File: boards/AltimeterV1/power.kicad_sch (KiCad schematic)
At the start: 36 parts

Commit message: updated hierarchical sheets and moved power schematics
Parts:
- removed BT?: Flight Computer Battery, Connector_JST:JST_PH_B2B-PH-K_1x02_P2.00mm_Vertical, symbol Device:Battery_Cell
- removed C?: 10uF, Capacitor_SMD:C_0805_2012Metric, symbol Device:C_Polarized_US
- removed C?: 2.2nF, Capacitor_SMD:C_0603_1608Metric, symbol Device:C
- removed C?: 2.27nF, Capacitor_SMD:C_0603_1608Metric, symbol Device:C
- removed C?: ~, Capacitor_SMD:C_0603_1608Metric, symbol Device:C
- removed C? (x2): 4.7u, Capacitor_SMD:C_0603_1608Metric, symbol Device:C
- removed C?: 47uF, Capacitor_SMD:C_0603_1608Metric, symbol Device:C
- removed C?, CByp?, CReg?, Cref?: 1uF, Capacitor_SMD:C_0603_1608Metric, symbol Device:C
- removed D? (x2): LED, LED_SMD:LED_0603_1608Metric, symbol Device:LED
- removed D?: D, Diode_SMD:D_0603_1608Metric, symbol Device:D
- removed D?: GREEN, LED_SMD:LED_0603_1608Metric, symbol Device:LED
- removed J?: TE_1776113-3, TerminalBlock_TE:TE_1776113-3, symbol Connector:Screw_Terminal_01x03
- removed R? (x4): 10k, Resistor_SMD:R_0603_1608Metric, symbol Device:R_US
- removed R?: 1k33, Resistor_SMD:R_0603_1608Metric, symbol Device:R_US
- removed R?: 432k, Resistor_SMD:R_0603_1608Metric, symbol Device:R_US
- removed R?: 5k6, Resistor_SMD:R_0603_1608Metric, symbol Device:R_US
- removed R?: 470k, Resistor_SMD:R_0603_1608Metric, symbol Device:R_US
- removed R?: 80k6, Resistor_SMD:R_0603_1608Metric, symbol Device:R_US
- removed R? (x3): 1k, Resistor_SMD:R_0603_1608Metric, symbol Device:R_US
- removed R?: 100k, Resistor_SMD:R_0603_1608Metric, symbol Device:R_US
- removed R?: 8.06k, Resistor_SMD:R_0603_1608Metric, symbol Device:R_US
- removed R?: 9.09k, Resistor_SMD:R_0603_1608Metric, symbol Device:R_US
- removed R?: 47k, Resistor_SMD:R_0603_1608Metric, symbol Device:R_US
- removed U?: ADP7158ACPZ-3.3-R7, Regulator_Linear:ADP7158ACPZ-3.3-R7, symbol regulator_analog:ADP7158ACPZ-3.3-R7
- removed U?: MCP73831-2-OT, Package_TO_SOT_SMD:SOT-23-5, symbol Battery_Management:MCP73831-2-OT
- removed U?: TPS2521, EFuse_Texas:TPS25210LRPWR, symbol Efuse_Texas_TPS2521:TPS2521
- added C? (x2): 1uF, Capacitor_SMD:C_0805_2012Metric, symbol D24V50F5:C
- added C?: 10nF, Capacitor_SMD:C_0805_2012Metric, symbol D24V50F5:C
- added J?: Conn_01x02_Female, symbol Connector:Conn_01x02_Female
- added U?: LD3985M33R_SOT23, Package_TO_SOT_SMD:SOT-23-5, symbol Regulator_Linear:LD3985M33R_SOT23
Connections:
- net +3V3: now also C?.1, U?.5 (VOUT)
- net GND: now also C?.1, C?.2, C?.2, J?.2 (Pin_2), U?.2 (GND)
- new net: C?.2, U?.4 (BYP)
- new net VBAT: C?.1, U?.1 (VIN)
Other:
- note added: "LD39 Linear Voltage Regulator"
- note added: "VBAT"
- note removed: "2.3V to 5.5V Input 3.3V Output"
- note removed: "2A Max Load"
- note removed: "Battery Switch Terminal"
- note removed: "Charger"
- note removed: "E-Fuse"
- note removed: "EN/UVLO must have large pullup resistor to prevent current leakage during reverse polarity. (350k or higher)"
- note removed: "Flight Battery Voltage Sensing"
- note removed: "Max Rating: Vin to GND = -0.3V to +7V"
- note removed: "OLD ALTIMETER POWER CIRCUIS"
- note removed: "OVCSEL Clamp Threshold Properties GND = 3.8V Open = 5.7V"
- note removed: "Protects: -15V to 28V Operates: 2.53V to 5.7V, 2.3A PowerGood Signal: V_IN > 2.7V"
- note removed: "Regulator"
- note removed: "Use calculator in datasheet for component values."
- note removed: "review resistance value choice with team (on 10k resistor)"

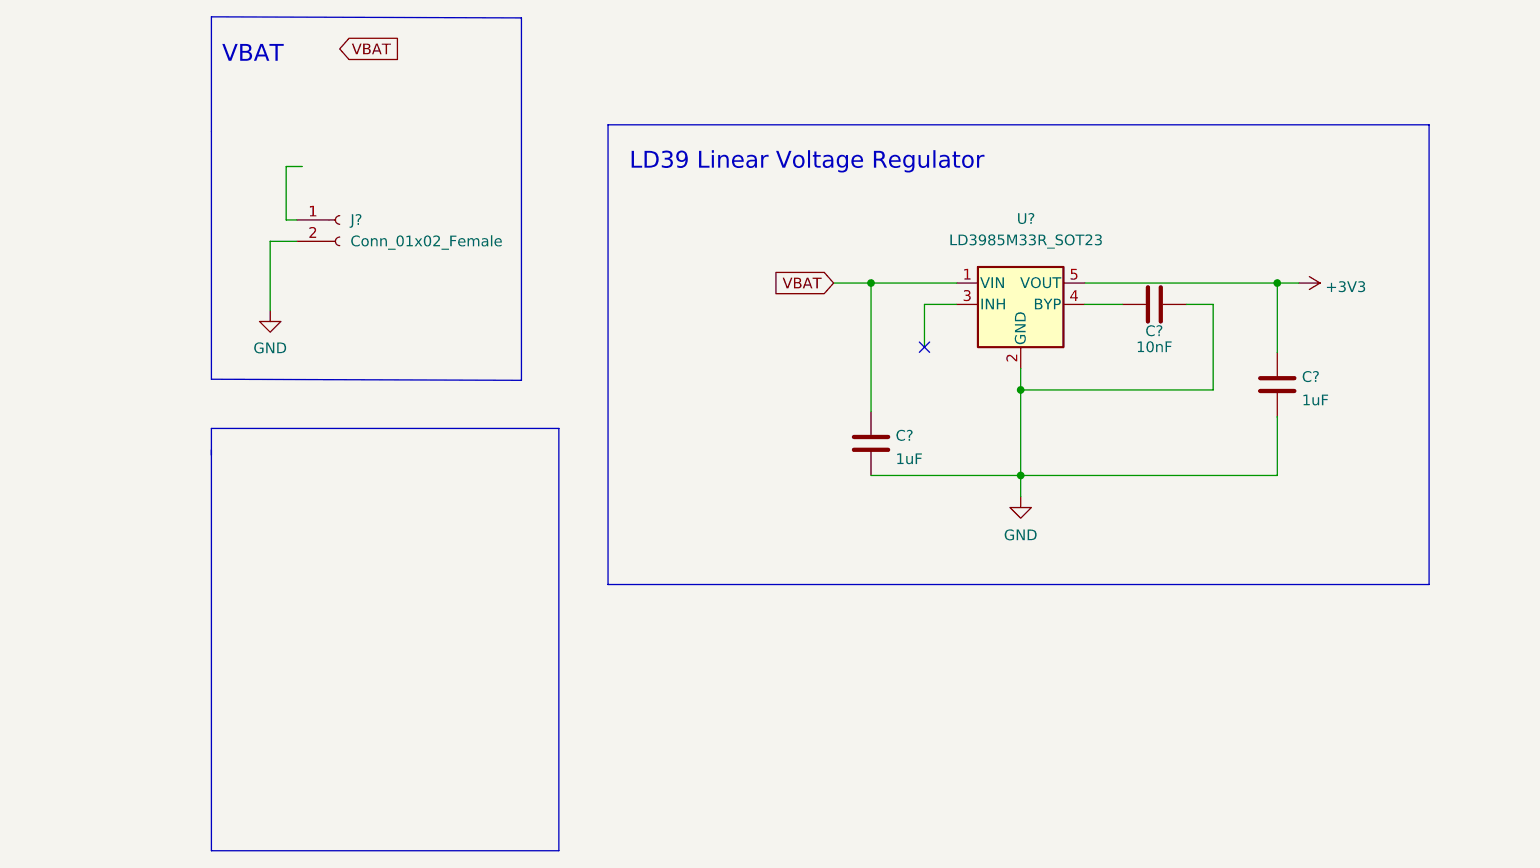
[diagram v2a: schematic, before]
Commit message: updated all schematics, and removed hierarchical sheets
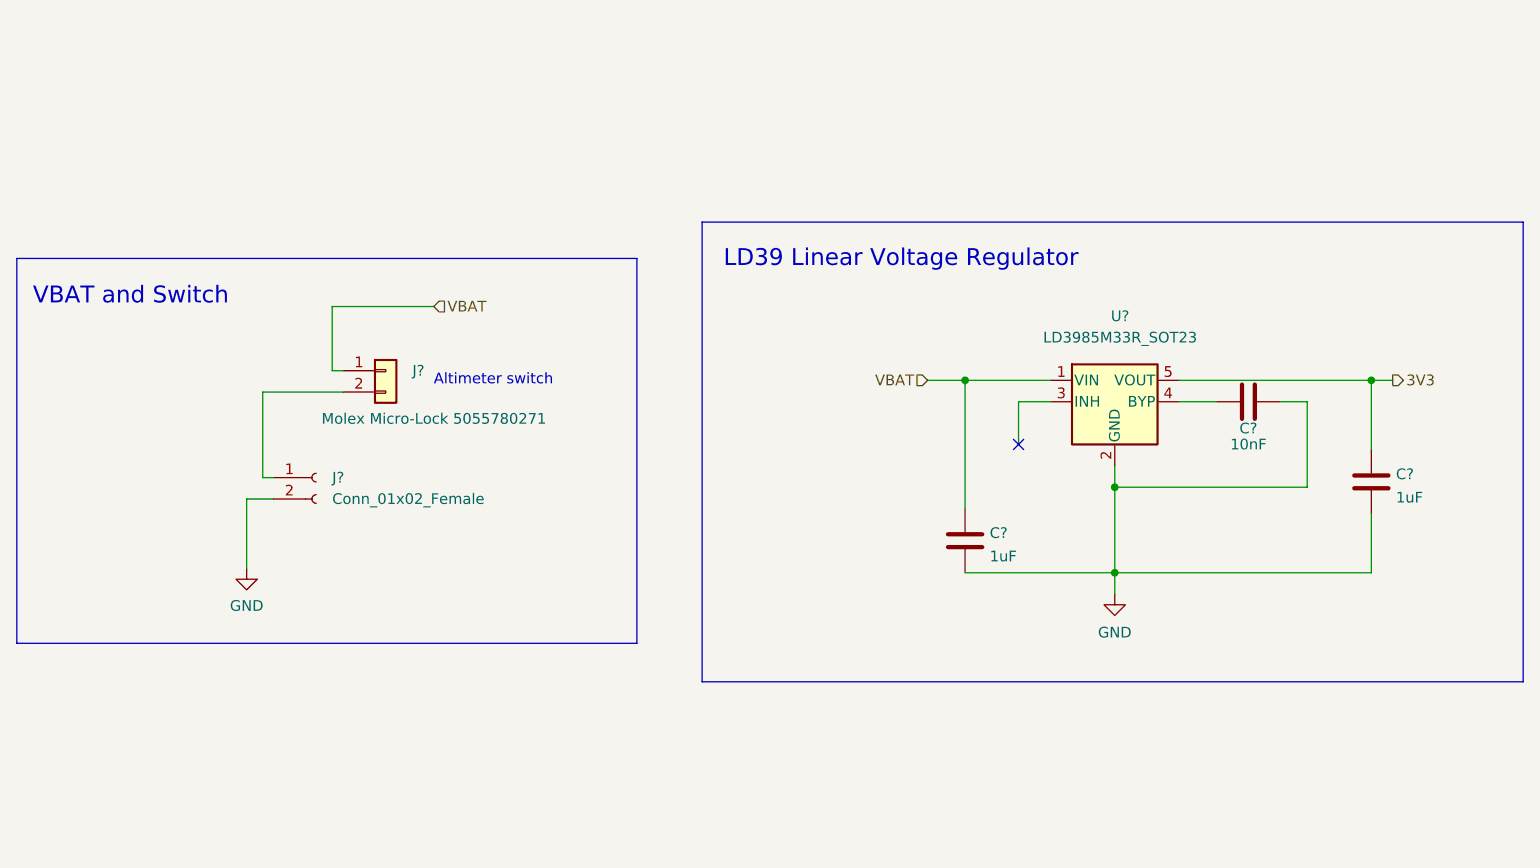
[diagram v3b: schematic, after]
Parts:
- added J?: Molex Micro-Lock 5055780271, Connector_Molex:Molex_CLIK-Mate_502494-0270_1x02-1MP_P2.00mm_Horizontal, symbol Connector_Generic:Conn_01x02
- J?: footprint (none) -> Connector_JST:JST_PH_B2B-PH-K_1x02_P2.00mm_Vertical
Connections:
- net VBAT: now also J?.1 (Pin_1)
- net at J?.1 (Pin_1): now also J?.2 (Pin_2)
- net +3V3 renamed 3V3
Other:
- note added: "Altimeter switch"
- note added: "VBAT and Switch"
- note removed: "VBAT"
- moved on the sheet: C?, J?, U?

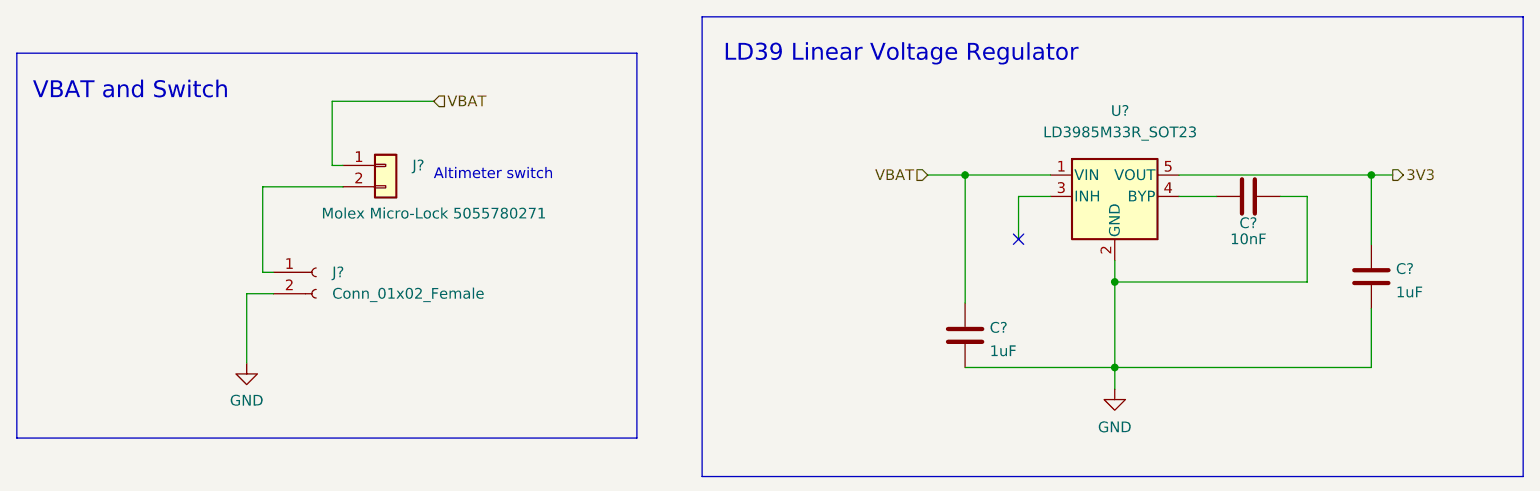
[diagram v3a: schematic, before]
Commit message: added flash memory, added buzzer, corrected all schematic labels, assigned footprints, added switch, updated pcb from schematic
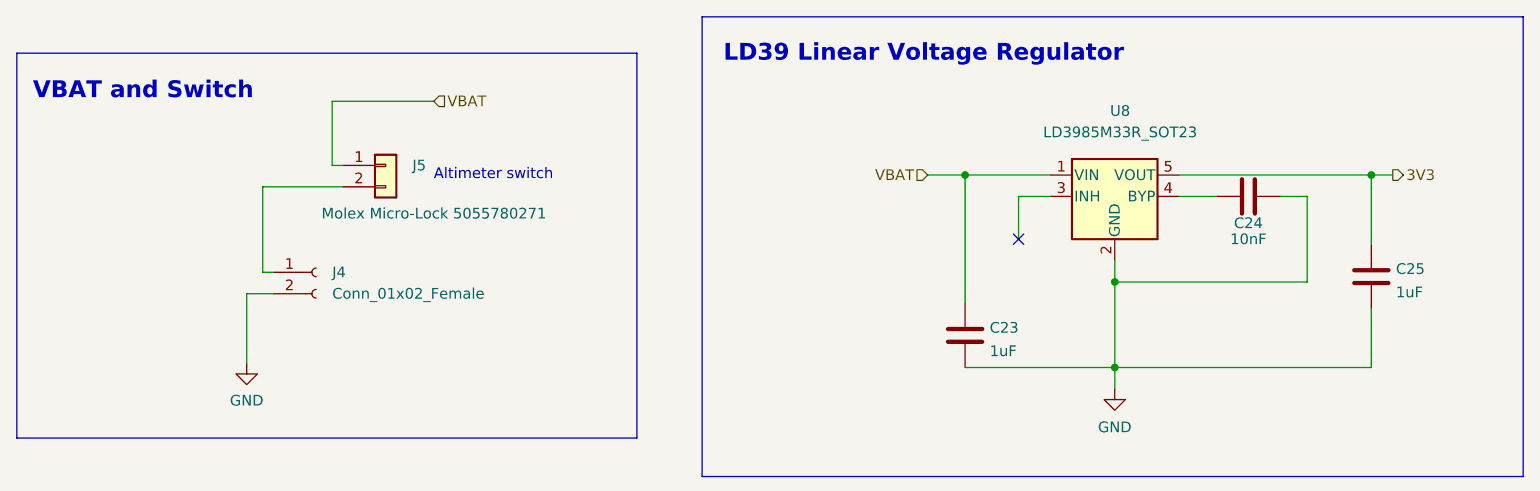
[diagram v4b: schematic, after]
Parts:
- gave numbers to parts that had none: 6
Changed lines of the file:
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@@
   )
   (text "LD39 Linear Voltage Regulator\n" (at 142.113 80.137 0)
-    (effects (font (size 2 2)) (justify left bottom))
+    (effects (font (size 2 2) (thickness 0.4) bold) (justify left bottom))
   )
   (text "VBAT and Switch" (at 60.071 84.582 0)
-    (effects (font (size 2 2)) (justify left bottom))
+    (effects (font (size 2 2) (thickness 0.4) bold) (justify left bottom))
   )
   (hierarchical_label "VBAT" (shape input) (at 166.37 93.345 180)
@@
   (symbol (lib_id "D24V50F5:C") (at 170.815 112.395 0) (unit 1)
     (in_bom yes) (on_board yes) (fields_autoplaced)
-    (property "Reference" "C?" (id 0) (at 173.736 111.4865 0)
+    (property "Reference" "C23" (id 0) (at 173.736 111.4865 0)
       (effects (font (size 1.27 1.27)) (justify left))
     )
@@
   (symbol (lib_id "Regulator_Linear:LD3985M33R_SOT23") (at 188.595 95.885 0) (unit 1)
     (in_bom yes) (on_board yes)
-    (property "Reference" "U?" (id 0) (at 189.23 85.725 0))
+    (property "Reference" "U8" (id 0) (at 189.23 85.725 0))
     (property "Value" "LD3985M33R_SOT23" (id 1) (at 189.23 88.265 0))
     (property "Footprint" "Package_TO_SOT_SMD:SOT-23-5" (id 2) (at 188.595 87.63 0)
@@
   (symbol (lib_id "D24V50F5:C") (at 219.075 105.41 0) (unit 1)
     (in_bom yes) (on_board yes) (fields_autoplaced)
-    (property "Reference" "C?" (id 0) (at 221.996 104.5015 0)
+    (property "Reference" "C25" (id 0) (at 221.996 104.5015 0)
       (effects (font (size 1.27 1.27)) (justify left))
     )
@@
   (symbol (lib_id "Connector:Conn_01x02_Female") (at 93.726 104.902 0) (unit 1)
     (in_bom yes) (on_board yes) (fields_autoplaced)
-    (property "Reference" "J?" (id 0) (at 95.631 104.9019 0)
+    (property "Reference" "J4" (id 0) (at 95.631 104.9019 0)
       (effects (font (size 1.27 1.27)) (justify left))
     )
@@
   (symbol (lib_id "Connector_Generic:Conn_01x02") (at 101.981 92.202 0) (unit 1)
     (in_bom yes) (on_board yes)
-    (property "Reference" "J?" (id 0) (at 105.156 92.2019 0)
+    (property "Reference" "J5" (id 0) (at 105.156 92.2019 0)
       (effects (font (size 1.27 1.27)) (justify left))
     )
@@
   (symbol (lib_id "power:GND") (at 85.471 115.697 0) (unit 1)
     (in_bom yes) (on_board yes) (fields_autoplaced)
-    (property "Reference" "#PWR?" (id 0) (at 85.471 122.047 0)
+    (property "Reference" "#PWR027" (id 0) (at 85.471 122.047 0)
       (effects (font (size 1.27 1.27)) hide)
     )
@@
   (symbol (lib_id "power:GND") (at 188.595 118.745 0) (unit 1)
     (in_bom yes) (on_board yes) (fields_autoplaced)
-    (property "Reference" "#PWR?" (id 0) (at 188.595 125.095 0)
+    (property "Reference" "#PWR028" (id 0) (at 188.595 125.095 0)
       (effects (font (size 1.27 1.27)) hide)
     )
@@
   (symbol (lib_id "D24V50F5:C") (at 204.47 95.885 270) (unit 1)
     (in_bom yes) (on_board yes)
-    (property "Reference" "C?" (id 0) (at 204.47 99.06 90))
+    (property "Reference" "C24" (id 0) (at 204.47 99.06 90))
     (property "Value" "10nF" (id 1) (at 204.47 100.965 90))
     (property "Footprint" "Capacitor_SMD:C_0805_2012Metric" (id 2) (at 200.66 96.8502 0)
